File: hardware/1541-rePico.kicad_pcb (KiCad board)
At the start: 2 copper layers, 59.1 x 60 mm, 44 parts, among them IC1 VIA6522, J1 Display Connector, J2 Display Power, J3 Conn_01x05_Pin, J4 SD Card Module Connector, J5 Conn_01x01_Pin, J6 EXT_5V, J7 RESET_1541, P1 VIA_PIN_1-20, P2 VIA_PIN_21-40, Q1 BSS138, Q2 BSS138, Q3 BSS138, Q4 BSS138, Q5 BSS138, Q6 BSS138, Q7 BSS138, Q8 BSS138, Q9 BSS138, SW1 RESET, U1 Pico, U2 SN74LVC4245A

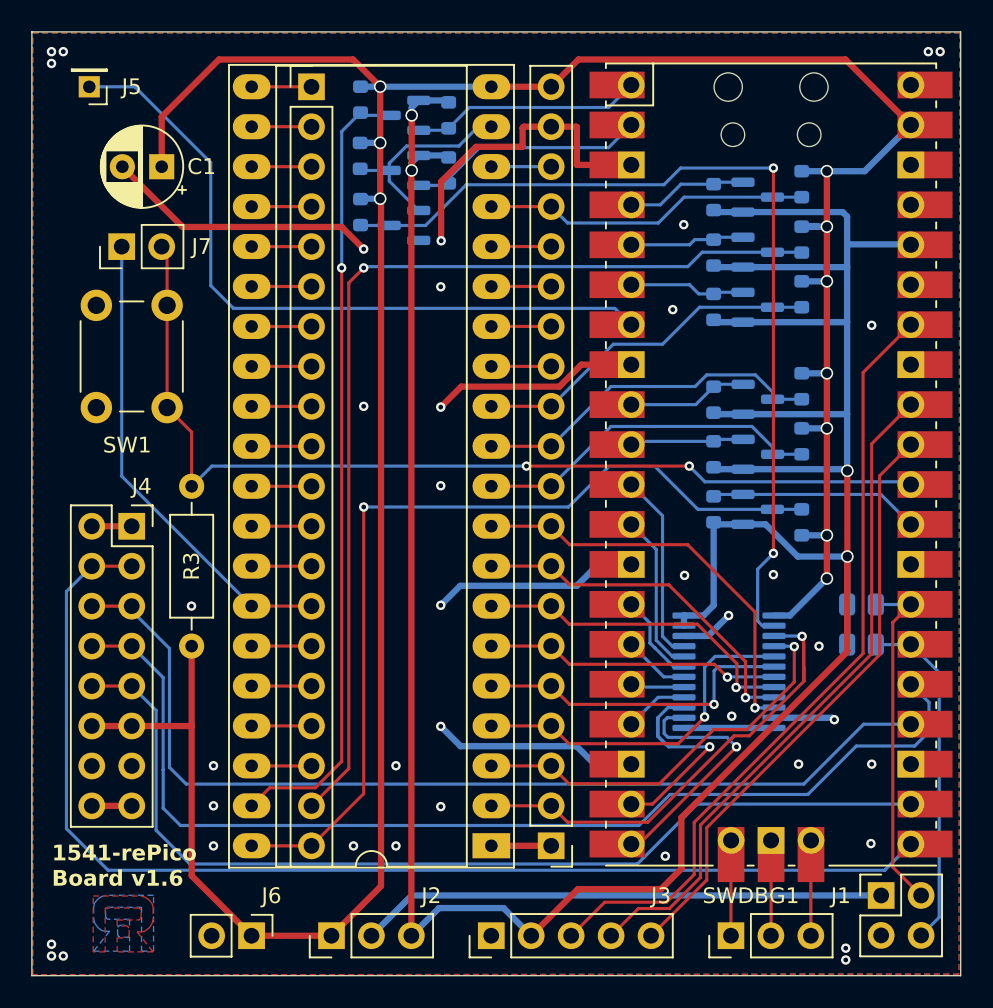
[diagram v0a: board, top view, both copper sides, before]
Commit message: modified PCB for Sound-connector
updated PCB to version 1.7
changes include:
- removal of SW-DBG header
- addition of Buzzer-connector
- changed layout of display-connector (straight vs. square)
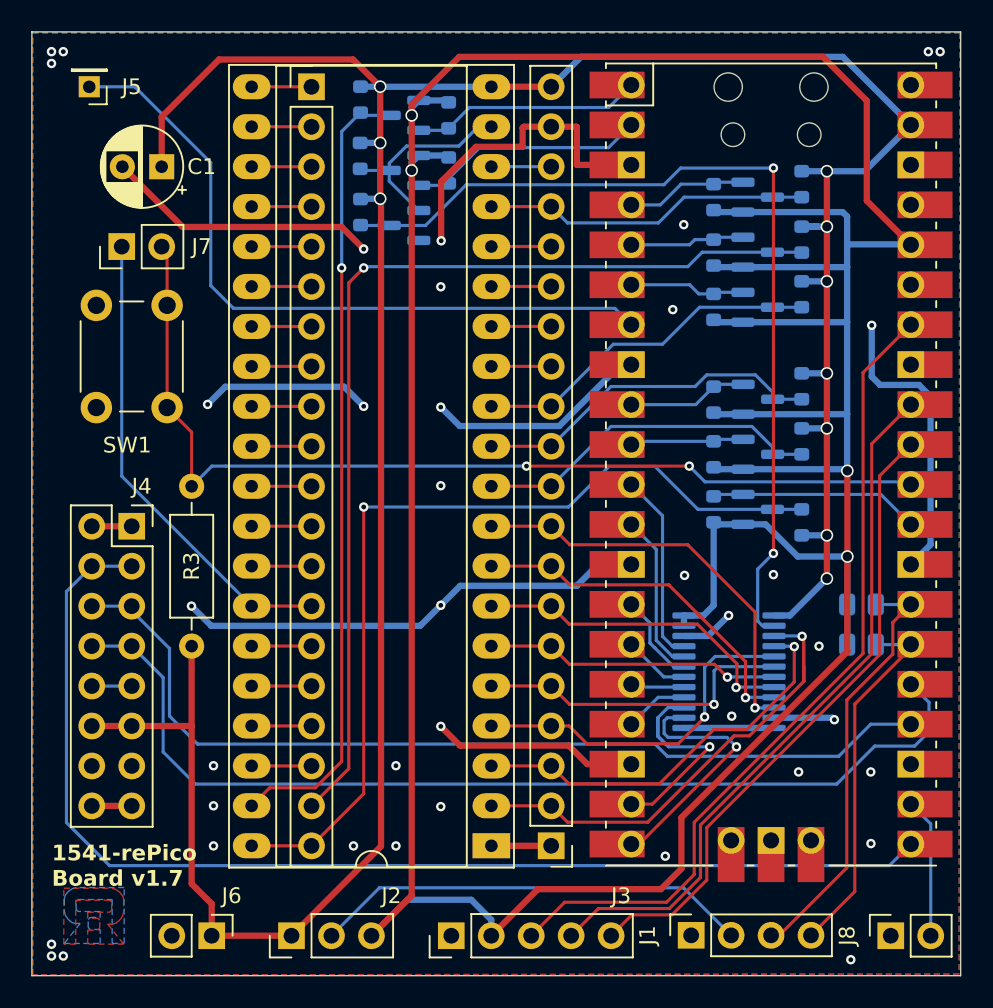
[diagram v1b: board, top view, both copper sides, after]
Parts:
- removed SWDBG1: DEBUG, Connector_PinHeader_2.54mm:PinHeader_1x03_P2.54mm_Vertical
- added J8: Buzzer Connector, Connector_PinSocket_2.54mm:PinSocket_1x02_P2.54mm_Vertical, F.Cu at (154.8, 122.5)
- J1: footprint Connector_PinSocket_2.54mm:PinSocket_2x02_P2.54mm_Vertical -> Connector_PinSocket_2.54mm:PinSocket_1x04_P2.54mm_Vertical
- moved J1 12.3 mm to (142.1, 122.5)
- moved J2 2.54 mm to (116.7, 122.5)
- moved J3 2.54 mm to (126.8, 122.5)
- moved J6 2.53 mm to (111.6, 122.5)
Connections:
- J1 pad 1: Net-(J1-Pin_1) -> GND
- J1 pad 2: GND -> Net-(J1-Pin_2)
- J2 pad 2: Net-(J1-Pin_1) -> Net-(J1-Pin_2)
- J4 pad 10: CS -> GND
- J4 pad 9: CS -> GND
- U1 pad 22: CS -> BUZZER+
- U1 pad 41: Net-(SWDBG1-Pin_1) -> unconnected-(U1-SWCLK-Pad41)
- U1 pad 42: Net-(SWDBG1-Pin_2) -> unconnected-(U1-GND-Pad42)
- U1 pad 43: Net-(SWDBG1-Pin_3) -> unconnected-(U1-SWDIO-Pad43)
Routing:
- net CS: track 62.8 -> 0.00 mm
- net GND: track 99.7 -> 152.1 mm
- net +3.3V: track 194.6 -> 241.6 mm
- net Net-(J1-Pin_1): track 33.5 -> 0.00 mm
- net Net-(J1-Pin_2): track 0.00 -> 27.9 mm
- net BUZZER+: track 0.00 -> 8.89 mm
- net Net-(SWDBG1-Pin_2): track 6.06 -> 0.00 mm
- net Net-(SWDBG1-Pin_3): track 6.06 -> 0.00 mm
- net Net-(SWDBG1-Pin_1): track 6.06 -> 0.00 mm
- net I2C_SCL: track 22.0 -> 27.3 mm
- net MOSI: track 68.8 -> 64.5 mm
- net SCK: track 62.9 -> 59.6 mm
- net Net-(J3-Pin_4): track 42.8 -> 45.4 mm
- net Net-(J3-Pin_5): track 38.1 -> 40.6 mm
- net Net-(J3-Pin_3): track 50.1 -> 52.6 mm
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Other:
- board text added: "1541-rePico Board v1.7"
- board text removed: "1541-rePico Board v1.6"
